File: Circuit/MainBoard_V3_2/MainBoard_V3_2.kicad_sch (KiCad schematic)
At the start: 141 parts, among them J1 Conn_01x02, J10 Conn_01x03, J11 Conn_01x03, J12 Conn_01x04, J13 Conn_01x04, J14 Conn_01x04, J15 Conn_01x04, J2 Conn_01x02, J3 Conn_01x02, J4 Conn_01x04, J5 Conn_01x02, J6 Conn_01x02, J7 Conn_01x02, J8 Conn_01x07, J9 Raspberry_Pi_2_3, Q1 Q_PMOS_GDS, Q10 BSS138, Q2 Q_PMOS_GDS, Q3 BSS138, Q4 IRLML6402, Q5 BSS138, Q6 BSS138, Q7 BSS138, Q8 BSS138, Q9 BSS138, SW1 SW_Push, SW2 SW_Push, SW3 SW_Push, SW4 SW_Slide_DPDT, SW5 SW_Slide_DPDT, U1 STM32F446RETx, U2 LM1117MP-3.3, U3 MPU-6050, U4 INA180A2, U5 INA180A2, Y1 CSTNE16M0V530000R0

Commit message: TVSダイオード追加
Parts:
- added D17, D18: SMAJ13A, Diode_SMD:D_SMA, symbol Diode:SMAJ13A
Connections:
- net GND: now also D18.2 (A2)
- net GNDP: now also D17.2 (A2)
- net VCC: now also D18.1 (A1)
- net VCCP: now also D17.1 (A1)
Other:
- moved on the sheet: D10, D11, D12, D13, NT1, R23, R24, R25, R26

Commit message: 修正多分最終
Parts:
- added C33, C34: 1uf, Capacitor_SMD:C_0603_1608Metric, symbol Device:C
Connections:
- net +3V3: now also C33.2, C34.2
- net GND: now also C33.1, C34.1
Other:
- moved on the sheet: C12, C13, C19, D14, R17, R18, R19, R20

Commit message: rasとstmをプルアップで繋げた
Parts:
- added R45: 10k, Resistor_SMD:R_0603_1608Metric, symbol Device:R
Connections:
- net +3V3: now also R45.2
- net RAS_SIG: now reaches U1.33 (PB12)
- net RAS_SIG: now also J9.31 (GCLK2/GPIO6), R45.1
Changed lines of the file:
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@@
 		)
 	)
+	(global_label "RAS_SIG"
+		(shape output)
+		(at 140.97 193.04 0)
+		(fields_autoplaced yes)
+		(effects
+			(font
+				(size 1.27 1.27)
+			)
+			(justify left)
+		)
+		(property "Intersheetrefs" "${INTERSHEET_REFS}"
+			(at 151.5752 193.04 0)
+			(effects
+				(font
+					(size 1.27 1.27)
+				)
+				(justify left)
+				(hide yes)
+			)
+		)
+	)
 	(global_label "BRAKE_LED"
 		(shape output)
@@
 		)
 	)
+	(global_label "RAS_SIG"
+		(shape input)
+		(at 345.44 113.03 0)
+		(fields_autoplaced yes)
+		(effects
+			(font
+				(size 1.27 1.27)
+			)
+			(justify left)
+		)
+		(property "Intersheetrefs" "${INTERSHEET_REFS}"
+			(at 356.0452 113.03 0)
+			(effects
+				(font
+					(size 1.27 1.27)
+				)
+				(justify left)
+				(hide yes)
+			)
+		)
+	)
 	(global_label "ENCODER_LEFT"
 		(shape output)
@@
 		)
 	)
+	(global_label "RAS_SIG"
+		(shape output)
+		(at 138.43 157.48 0)
+		(fields_autoplaced yes)
+		(effects
+			(font
+				(size 1.27 1.27)
+			)
+			(justify left)
+		)
+		(property "Intersheetrefs" "${INTERSHEET_REFS}"
+			(at 149.0352 157.48 0)
+			(effects
+				(font
+					(size 1.27 1.27)
+				)
+				(justify left)
+				(hide yes)
+			)
+		)
+	)
 	(global_label "STM_LED1"
 		(shape input)
@@
 	)
 	(symbol
+		(lib_id "Device:R")
+		(at 134.62 157.48 270)
+		(unit 1)
+		(exclude_from_sim no)
+		(in_bom yes)
+		(on_board yes)
+		(dnp no)
+		(property "Reference" "R45"
+			(at 134.62 157.48 90)
+			(effects
+				(font
+					(size 1.27 1.27)
+				)
+			)
+		)
+		(property "Value" "10k"
+			(at 134.62 160.02 90)
+			(effects
+				(font
+					(size 1.27 1.27)
+				)
+			)
+		)
+		(property "Footprint" "Resistor_SMD:R_0603_1608Metric"
+			(at 134.62 155.702 90)
+			(effects
+				(font
+					(size 1.27 1.27)
+				)
+				(hide yes)
+			)
+		)
+		(property "Datasheet" "~"
+			(at 134.62 157.48 0)
+			(effects
+				(font
+					(size 1.27 1.27)
+				)
+				(hide yes)
+			)
+		)
+		(property "Description" "Resistor"
+			(at 134.62 157.48 0)
+			(effects
+				(font
+					(size 1.27 1.27)
+				)
+				(hide yes)
+			)
+		)
+		(pin "1"
+		)
+		(pin "2"
+		)
+		(instances
+			(project "MainBoard_V3_2"
+				(path "/82c1f385-b98b-40ef-9728-ce204bc5c807"
+					(reference "R45")
+					(unit 1)
+				)
+			)
+		)
+	)
+	(symbol
 		(lib_id "power:GND")
 		(at 43.18 130.81 0)
@@
 					(unit 1)
 				)
+			)
+		)
+	)
+	(symbol
+		(lib_id "power:+3V3")
+		(at 130.81 157.48 0)
+		(unit 1)
+		(exclude_from_sim no)
+		(in_bom yes)
+		(on_board yes)
+		(dnp no)
+		(property "Reference" "#PWR048"
+			(at 130.81 161.29 0)
+			(effects
+				(font
+					(size 1.27 1.27)
+				)
+				(hide yes)
+			)
+		)
+		(property "Value" "+3V3"
+			(at 130.81 153.67 0)
+			(effects
+				(font
+					(size 1.27 1.27)
+				)
+			)
+		)
+		(property "Footprint" ""
+			(at 130.81 157.48 0)
+			(effects
+				(font
+					(size 1.27 1.27)
+				)
+				(hide yes)
+			)
+		)
+		(property "Datasheet" ""
+			(at 130.81 157.48 0)
+			(effects
+				(font
+					(size 1.27 1.27)
+				)
+				(hide yes)
+			)
+		)
+		(property "Description" "Power symbol creates a global label with name \"+3V3\""
+			(at 130.81 157.48 0)
+			(effects
+				(font
+					(size 1.27 1.27)
+				)
+				(hide yes)
+			)
+		)
+		(pin "1"
+		)
+		(instances
+			(project "MainBoard_V3_2"
+				(path "/82c1f385-b98b-40ef-9728-ce204bc5c807"
+					(reference "#PWR048")
+					(unit 1)
+				)

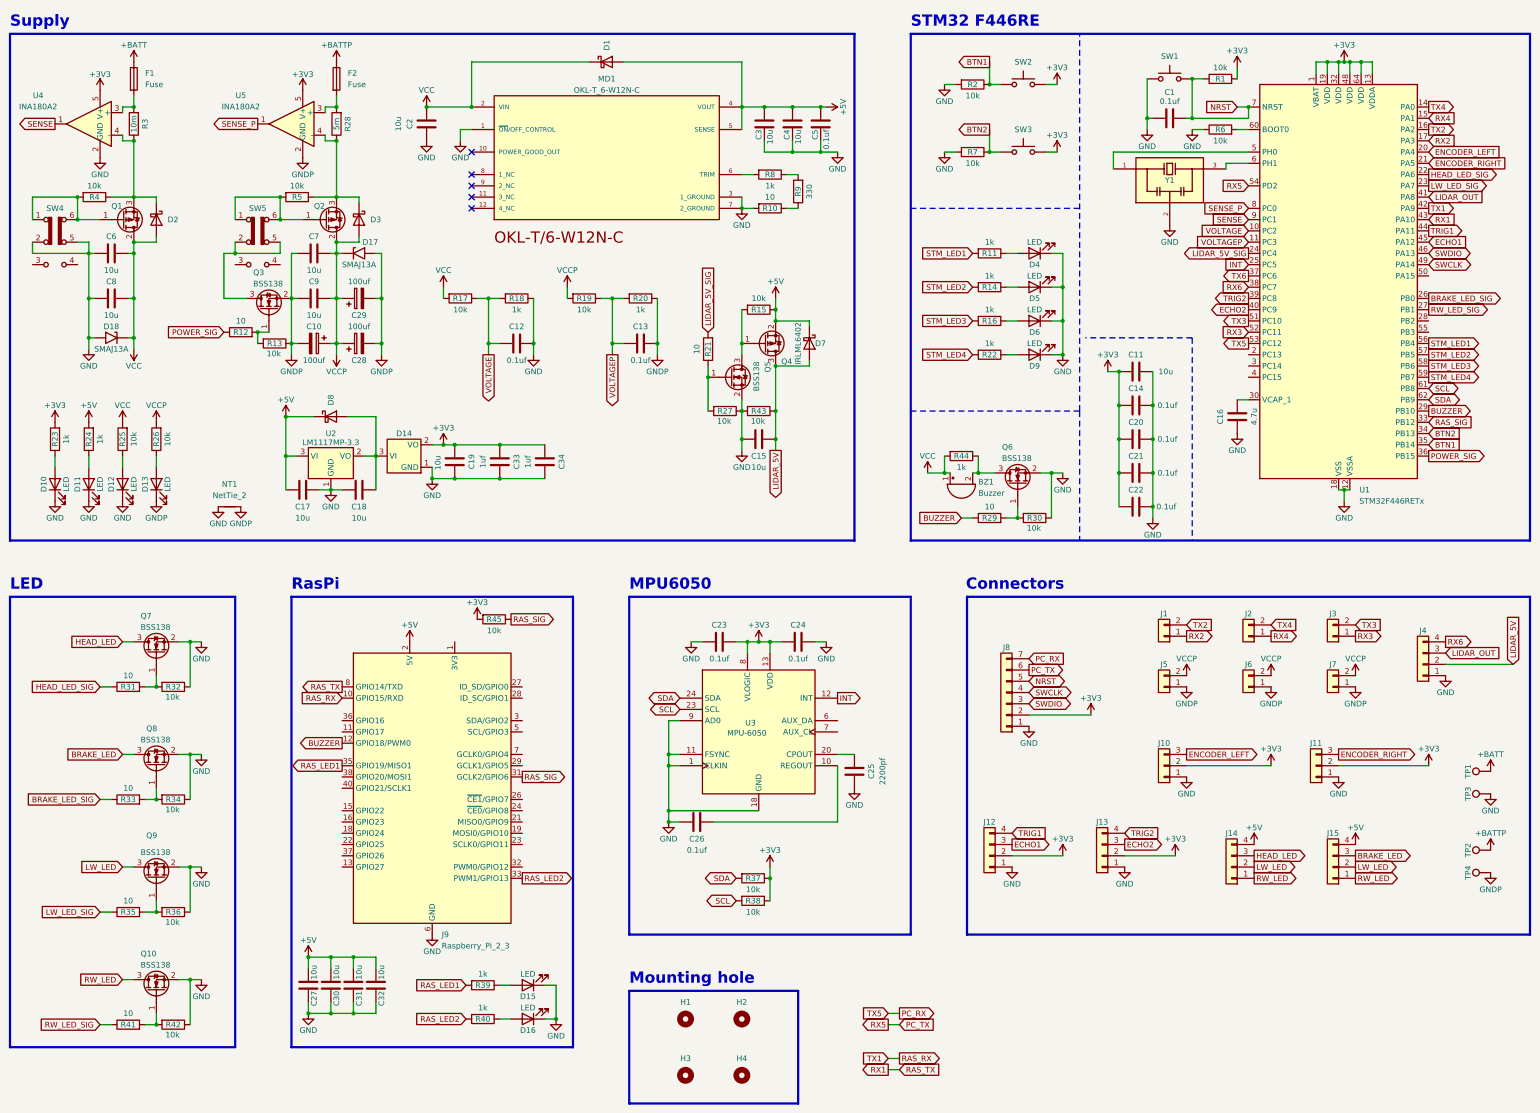
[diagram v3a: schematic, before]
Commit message: fableに聞いて修正（コンデンサ追加など）
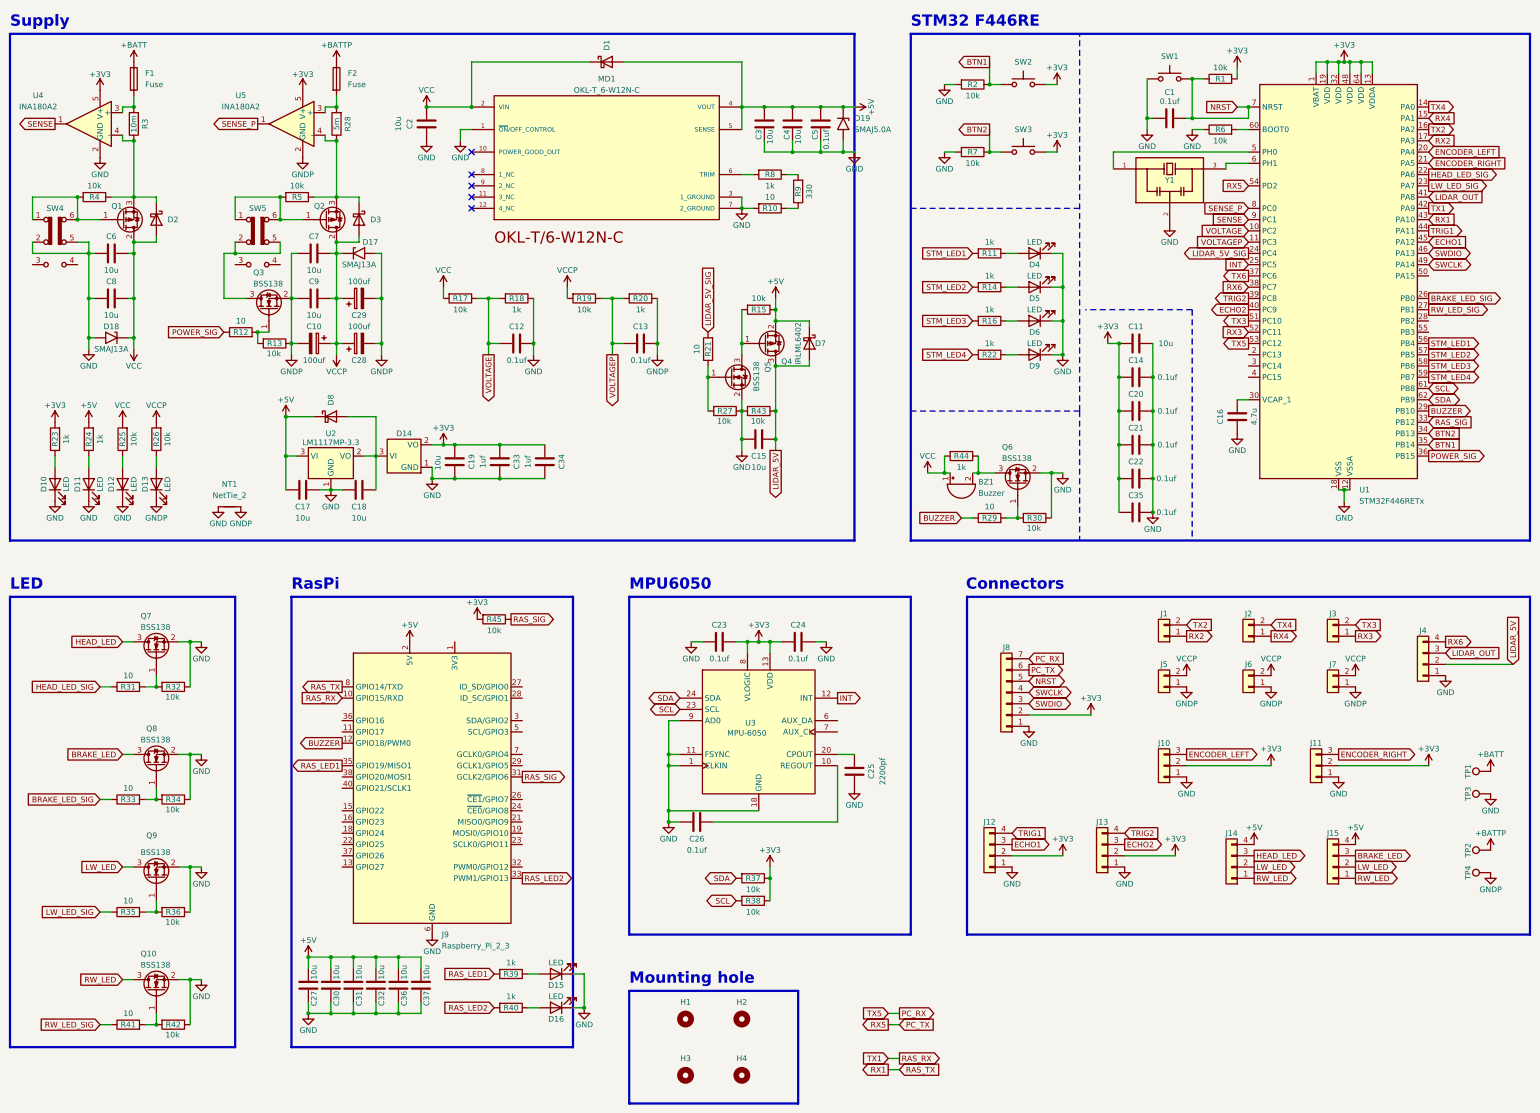
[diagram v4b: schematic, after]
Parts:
- added C35: 0.1uf, Capacitor_SMD:C_0603_1608Metric, symbol Device:C
- added C36, C37: 10u, Capacitor_SMD:C_0805_2012Metric, symbol Device:C
- added D19: SMAJ5.0A, Diode_SMD:D_SMA, symbol Diode:SMAJ5.0A
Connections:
- net +3V3: now also C35.2
- net +5V: now also C36.1, C37.1, D19.1 (A1)
- net GND: now also C35.1, C36.2, C37.2, D19.2 (A2)
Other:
- moved on the sheet: C11, C14, C20, C21, C22, D15, D16, R39, R40
